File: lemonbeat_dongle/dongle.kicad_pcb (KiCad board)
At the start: 4 copper layers, 50 x 20 mm, 81 parts, among them J201 USB_A, J202 Prog, J203 u.FL, J301 SMA, SW201 SW_Push, U201 nRF52840, U301 Si4467, Y201 32MHz, Y202 32.768kHz, Y301 26MHz

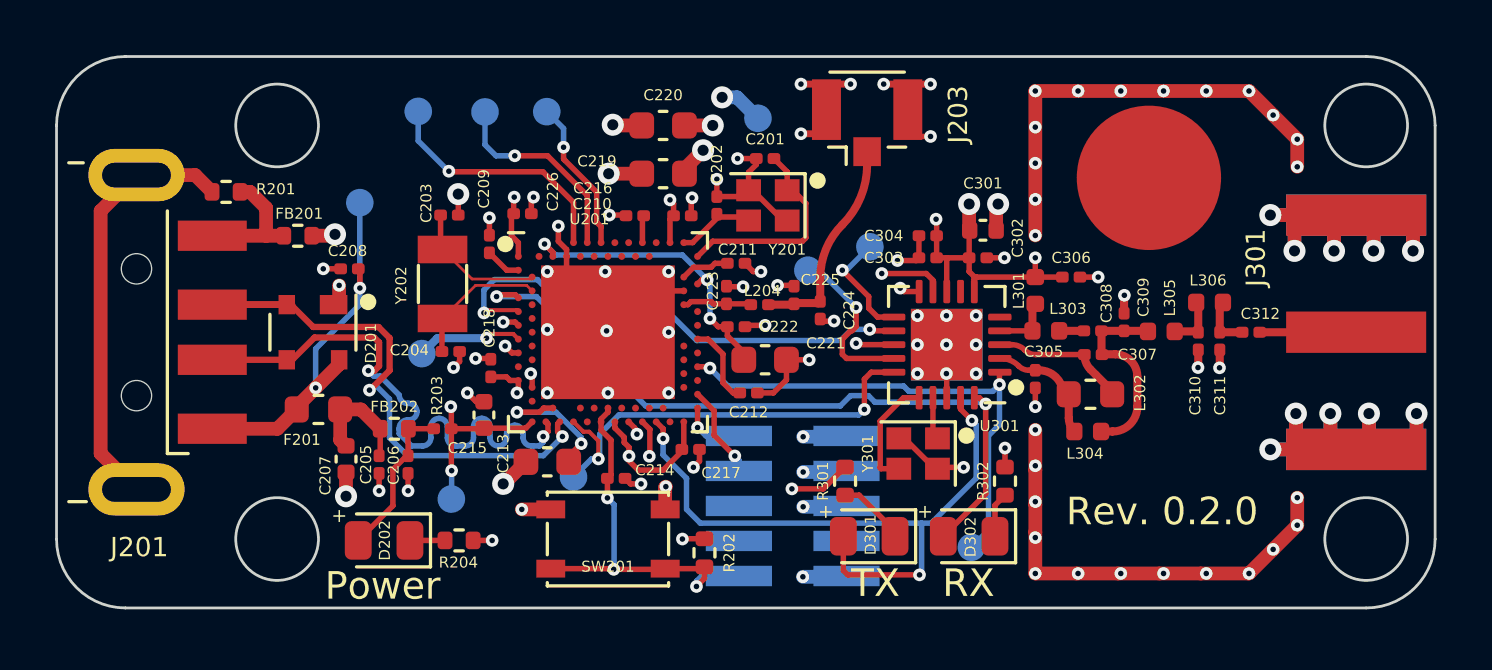
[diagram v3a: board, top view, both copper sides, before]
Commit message: dongle: PCB: move components further away from holes
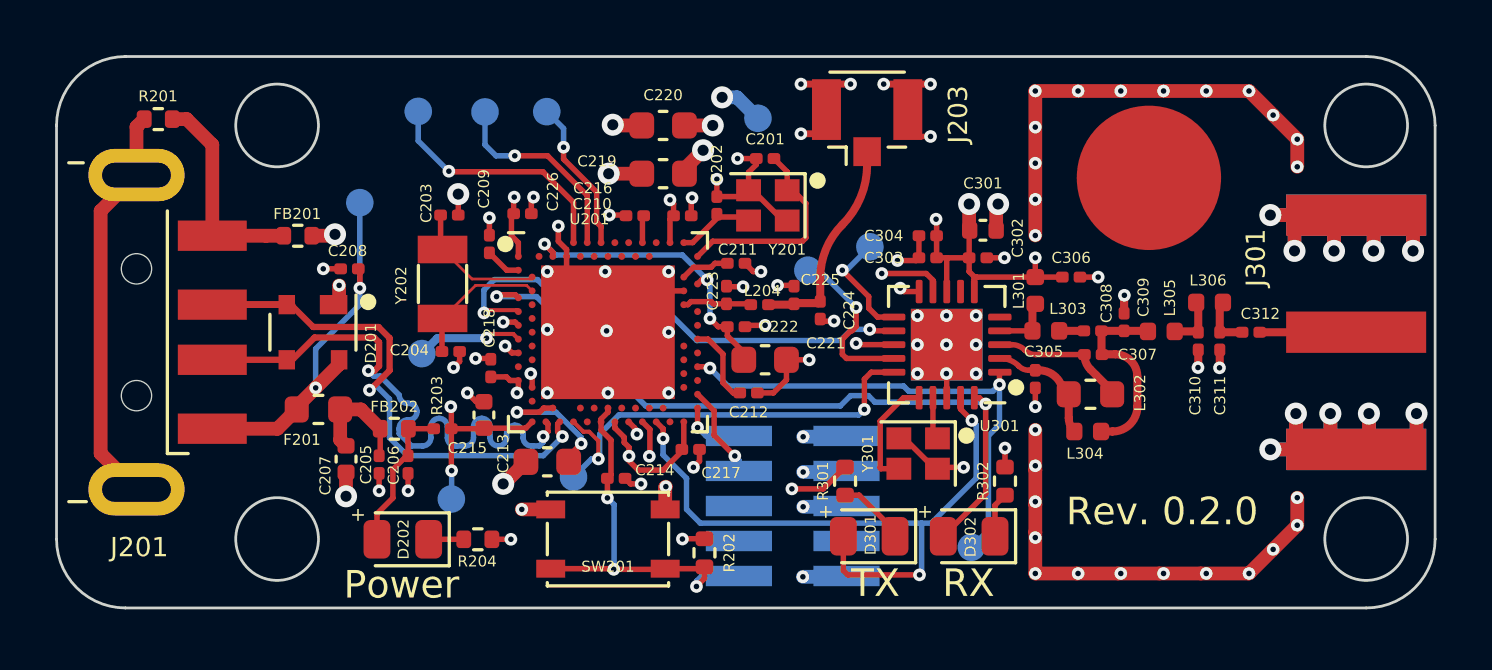
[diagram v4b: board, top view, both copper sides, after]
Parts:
- moved R201 3.61 mm to (114.2, 96.3)
- moved D202 0.68 mm to (123.1, 111.5)
- moved R204 0.68 mm to (125.8, 111.5)
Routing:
- net Net-(FB201-Pad1): track 4.58 -> 7.53 mm
- net Net-(J201-Pad5): track 15.5 -> 14.6 mm
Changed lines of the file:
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@@
   )
   (footprint "LED_SMD:LED_0805_2012Metric" (layer "F.Cu")
-    (at 122.38 111.55 180)
+    (at 123.06 111.51 180)
     (descr "LED SMD 0805 (2012 Metric), square (rectangular) end terminal, IPC_7351 nominal, (Body size source: https://docs.google.com/spreadsheets/d/1BsfQQcO9C6DZCsRaXUlFlo91Tg2WpOkGARC1WS5S8t0/edit?usp=sharing), generated with kicad-footprint-generator")
     (tags "LED")
@@
   )
   (footprint "Resistor_SMD:R_0402_1005Metric" (layer "F.Cu")
-    (at 125.1 111.55)
+    (at 125.78 111.51)
     (descr "Resistor SMD 0402 (1005 Metric), square (rectangular) end terminal, IPC_7351 nominal, (Body size source: IPC-SM-782 page 72, https://www.pcb-3d.com/wordpress/wp-content/uploads/ipc-sm-782a_amendment_1_and_2.pdf), generated with kicad-footprint-generator")
     (tags "resistor")
@@
   )
   (footprint "Resistor_SMD:R_0402_1005Metric" (layer "F.Cu")
-    (at 116.65 98.91)
+    (at 114.19 96.27)
     (descr "Resistor SMD 0402 (1005 Metric), square (rectangular) end terminal, IPC_7351 nominal, (Body size source: IPC-SM-782 page 72, https://www.pcb-3d.com/wordpress/wp-content/uploads/ipc-sm-782a_amendment_1_and_2.pdf), generated with kicad-footprint-generator")
     (tags "resistor")
@@
     (property "Sheetname" "MCU")
     (attr smd)
-    (fp_text reference "R201" (at 1.8 -0.1) (layer "F.SilkS")
+    (fp_text reference "R201" (at -0.01 -0.83) (layer "F.SilkS")
       (effects (font (size 0.4 0.4) (thickness 0.1)))
     )
@@
     (property "Sheetname" "MCU")
     (attr smd)
-    (fp_text reference "FB201" (at 0.05 -0.8) (layer "F.SilkS")
+    (fp_text reference "FB201" (at -0.02 -0.79) (layer "F.SilkS")
       (effects (font (size 0.4 0.4) (thickness 0.1)))
     )
@@
   (gr_arc (start 160.5 111.5) (mid 159.767767 113.267767) (end 158 114) (layer "Edge.Cuts") (width 0.1))
   (gr_line (start 113 94) (end 158 94) (layer "Edge.Cuts") (width 0.1))
-  (gr_text "Power" (at 122.33 113.2) (layer "F.SilkS")
+  (gr_text "Power" (at 123.01 113.16) (layer "F.SilkS")
     (effects (font (size 1 1) (thickness 0.15)))
   )
-  (gr_text "+" (at 120.755 110.65) (layer "F.SilkS")
+  (gr_text "+" (at 121.435 110.61) (layer "F.SilkS")
     (effects (font (size 0.5 0.5) (thickness 0.1)))
   )
@@
   (segment (start 142.7875 106.375) (end 142.7875 105.4875) (width 0.2) (layer "F.Cu") (net 1))
   (segment (start 142.7875 105.3125) (end 142.7875 104.45) (width 0.2) (layer "F.Cu") (net 1))
-  (segment (start 126.3 111.55) (end 125.61 111.55) (width 0.2) (layer "F.Cu") (net 1))
+  (segment (start 126.98 111.51) (end 126.29 111.51) (width 0.2) (layer "F.Cu") (net 1))
   (segment (start 120.7 101.7) (end 120.75 101.75) (width 0.2) (layer "F.Cu") (net 1))
   (segment (start 127.72 99.18) (end 127.8 99.1) (width 0.2) (layer "F.Cu") (net 1))
@@
   (via (at 154.625 111.875) (size 0.46) (drill 0.2) (layers "F.Cu" "B.Cu") (free) (net 1))
   (via (at 125.7 104.95) (size 0.46) (drill 0.2) (layers "F.Cu" "B.Cu") (free) (net 1))
-  (via (at 126.3 111.55) (size 0.46) (drill 0.2) (layers "F.Cu" "B.Cu") (free) (net 1))
+  (via (at 126.98 111.51) (size 0.46) (drill 0.2) (layers "F.Cu" "B.Cu") (free) (net 1))
   (via (at 126.2 99.85) (size 0.46) (drill 0.2) (layers "F.Cu" "B.Cu") (free) (net 1))
   (via (at 136.05 101.8) (size 0.46) (drill 0.2) (layers "F.Cu" "B.Cu") (free) (net 1))
@@
   (segment (start 120.7875 106.8) (end 120.7875 107.9075) (width 0.5) (layer "F.Cu") (net 6))
   (segment (start 123.25 107.51) (end 123.26 107.5) (width 0.2) (layer "F.Cu") (net 7))
-  (segment (start 122.7 108.977552) (end 122.7 110.2925) (width 0.2) (layer "F.Cu") (net 7))
-  (segment (start 122.7 110.2925) (end 121.4425 111.55) (width 0.2) (layer "F.Cu") (net 7))
+  (segment (start 122.7 108.977552) (end 123.197552 108.48) (width 0.2) (layer "F.Cu") (net 7))
+  (segment (start 122.1225 110.5875) (end 122.7 110.01) (width 0.2) (layer "F.Cu") (net 7))
   (segment (start 123.26 107.5) (end 124.18 107.5) (width 0.2) (layer "F.Cu") (net 7))
   (segment (start 123.25 108.48) (end 123.25 107.51) (width 0.2) (layer "F.Cu") (net 7))
-  (segment (start 123.197552 108.48) (end 122.7 108.977552) (width 0.2) (layer "F.Cu") (net 7))
+  (segment (start 122.1225 111.51) (end 122.1225 110.5875) (width 0.2) (layer "F.Cu") (net 7))
+  (segment (start 122.7 110.01) (end 122.7 108.977552) (width 0.2) (layer "F.Cu") (net 7))
   (segment (start 119.2125 106.8) (end 119.2125 106.704908) (width 0.5) (layer "F.Cu") (net 8))
   (segment (start 120.75 105) (end 120.75 105.167408) (width 0.5) (layer "F.Cu") (net 8))
@@
   (segment (start 122.094359 105.943545) (end 122.006455 105.943545) (width 0.2) (layer "B.Cu") (net 28))
   (segment (start 116.35 100.5) (end 118.1 100.5) (width 0.5) (layer "F.Cu") (net 29))
-  (segment (start 117.52 98.91) (end 117.16 98.91) (width 0.5) (layer "F.Cu") (net 29))
-  (segment (start 118.1 99.49) (end 117.52 98.91) (width 0.5) (layer "F.Cu") (net 29))
-  (segment (start 118.1 100.5) (end 118.1 99.49) (width 0.5) (layer "F.Cu") (net 29))
+  (segment (start 115.22 96.27) (end 116.15 97.2) (width 0.5) (layer "F.Cu") (net 29))
+  (segment (start 114.7 96.27) (end 115.22 96.27) (width 0.5) (layer "F.Cu") (net 29))
+  (segment (start 116.15 97.2) (end 116.15 100.5) (width 0.5) (layer "F.Cu") (net 29))
   (segment (start 118.1 100.5) (end 118.74 100.5) (width 0.5) (layer "F.Cu") (net 29))
   (segment (start 112.1 99.6) (end 113.4 98.3) (width 0.5) (layer "F.Cu") (net 30))
   (segment (start 113.4 109.7) (end 112.1 108.4) (width 0.5) (layer "F.Cu") (net 30))
-  (segment (start 115.53 98.3) (end 116.14 98.91) (width 0.5) (layer "F.Cu") (net 30))
+  (segment (start 113.4 96.55) (end 113.68 96.27) (width 0.5) (layer "F.Cu") (net 30))
   (segment (start 112.1 108.4) (end 112.1 99.6) (width 0.5) (layer "F.Cu") (net 30))
-  (segment (start 113.4 98.3) (end 115.53 98.3) (width 0.5) (layer "F.Cu") (net 30))
+  (segment (start 113.4 98.3) (end 113.4 96.55) (width 0.5) (layer "F.Cu") (net 30))
   (segment (start 133.75 107.4565) (end 133.75 106.75) (width 0.2) (layer "F.Cu") (net 31))
   (via (at 133.75 107.4565) (size 0.46) (drill 0.2) (layers "F.Cu" "B.Cu") (net 31))
@@
   (segment (start 140.777 104.231744) (end 139.824744 105.184) (width 0.2) (layer "In2.Cu") (net 39))
   (segment (start 138.852256 104.861) (end 138.639 104.861) (width 0.2) (layer "In2.Cu") (net 39))
-  (segment (start 123.3175 111.55) (end 124.59 111.55) (width 0.2) (layer "F.Cu") (net 40))
+  (segment (start 123.9975 111.51) (end 125.27 111.51) (width 0.2) (layer "F.Cu") (net 40))
   (segment (start 140.9125 111.4) (end 140.9125 111.2125) (width 0.2) (layer "F.Cu") (net 41))
   (segment (start 139.61 109.91) (end 139.1 109.91) (width 0.2) (layer "F.Cu") (net 41))

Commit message: dongle: schematic & PCB: nRF52840 oscillator changes
- change footprint of capacitors for both crystals to 0402 so they can
  be exchanged more easily
- rotate Y201 for better symmetry
- no ground plane keepout area below crystals
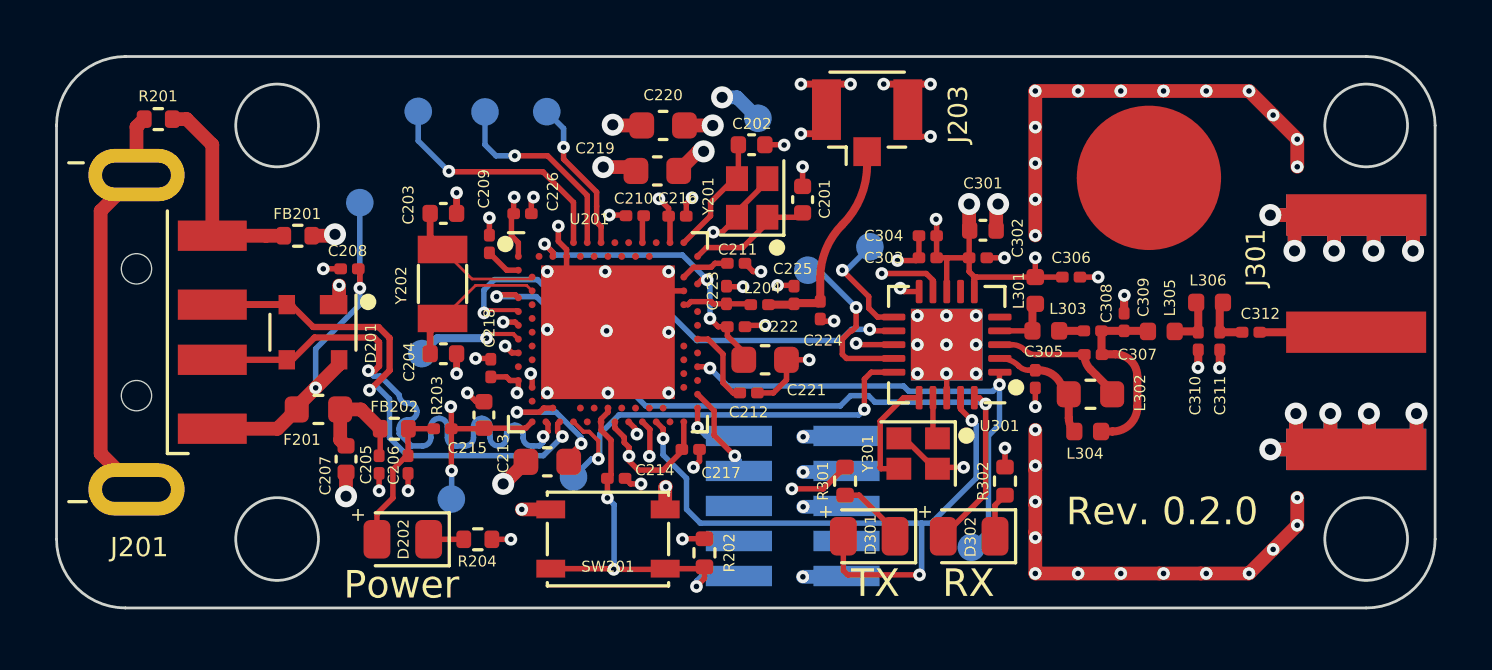
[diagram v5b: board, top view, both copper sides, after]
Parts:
- C201, C202, C203, C204: footprint Capacitor_SMD:C_0201_0603Metric -> Capacitor_SMD:C_0402_1005Metric
- moved C202 2.54 mm to (135.7, 97.2), turned to 180 degrees
- moved C201 2.02 mm to (137.6, 99.2), turned to -90 degrees
- moved Y201 0.63 mm to (135.7, 99.1), turned to 90 degrees
- moved C204 0.28 mm to (124.5, 104.8)
- moved C219 0.23 mm to (132.3, 98.2)
- moved C203 0.23 mm to (124.5, 99.7)
- moved C216 0.18 mm to (133.0, 99.8)
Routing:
- net Net-(C201-Pad2): track 7.68 -> 4.58 mm
- net Net-(C202-Pad2): track 2.79 -> 4.43 mm
- net GND: track 121.8 -> 120.7 mm, vias 105 -> 106

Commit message: dongle: add test point for SWDCLK & space test points further apart
This should allow creating a test jig even with test pads of 2mm
diameter.
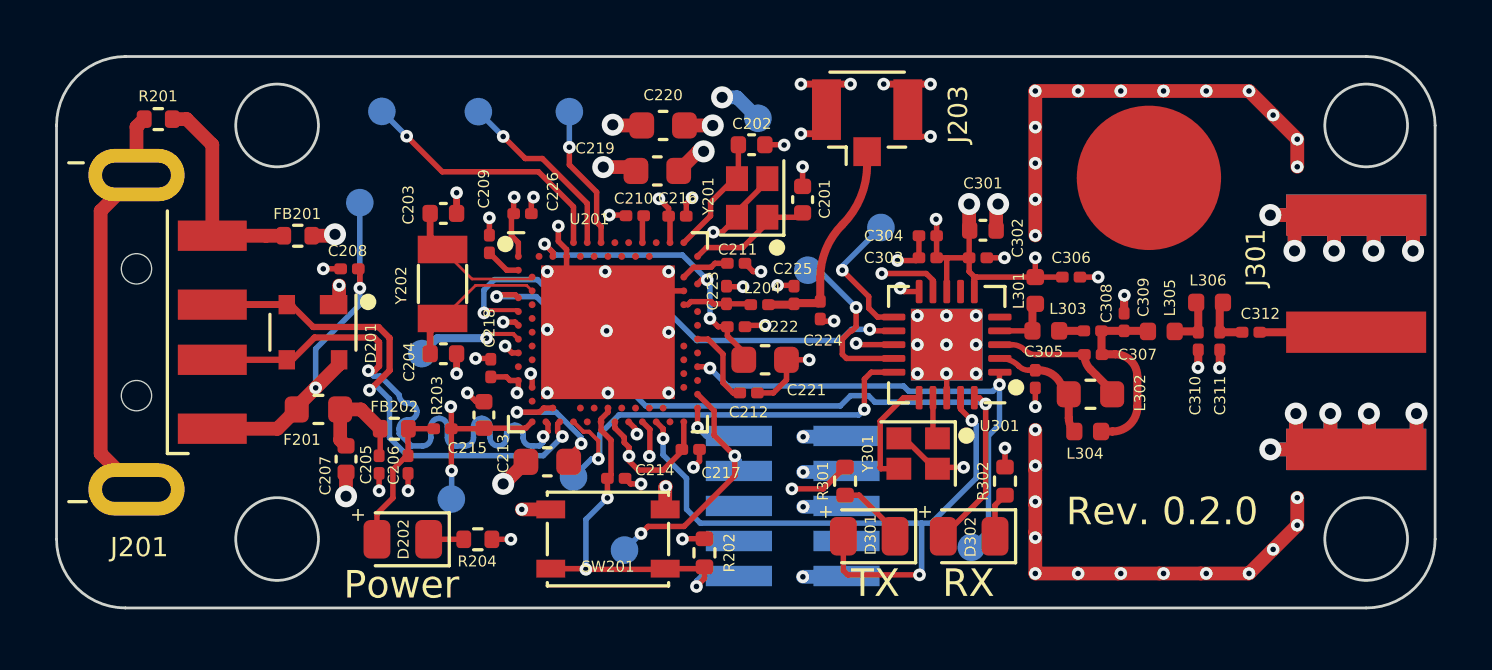
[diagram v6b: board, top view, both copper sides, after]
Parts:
- added TP207: TestPoint, TestPoint:TestPoint_Pad_D1.0mm, B.Cu at (131.1, 111.9)
- moved TP206 1.32 mm to (122.3, 96.0)
- moved TP204 0.82 mm to (129.1, 96.0)
- moved TP106 0.81 mm to (140.4, 100.2)
- moved TP205 0.24 mm to (125.8, 96.0)
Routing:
- net /MCU/SWDCLK: track 3.40 -> 9.24 mm, vias 1 -> 2
- net /MCU/P1.09: track 19.0 -> 19.7 mm
- net Net-(TP205-Pad1): track 7.37 -> 6.75 mm
- net Net-(TP206-Pad1): track 9.08 -> 9.68 mm

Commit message: dongle: update schematics & PCBs to KiCAD 7 & fix ERC/DRC errors & warnings
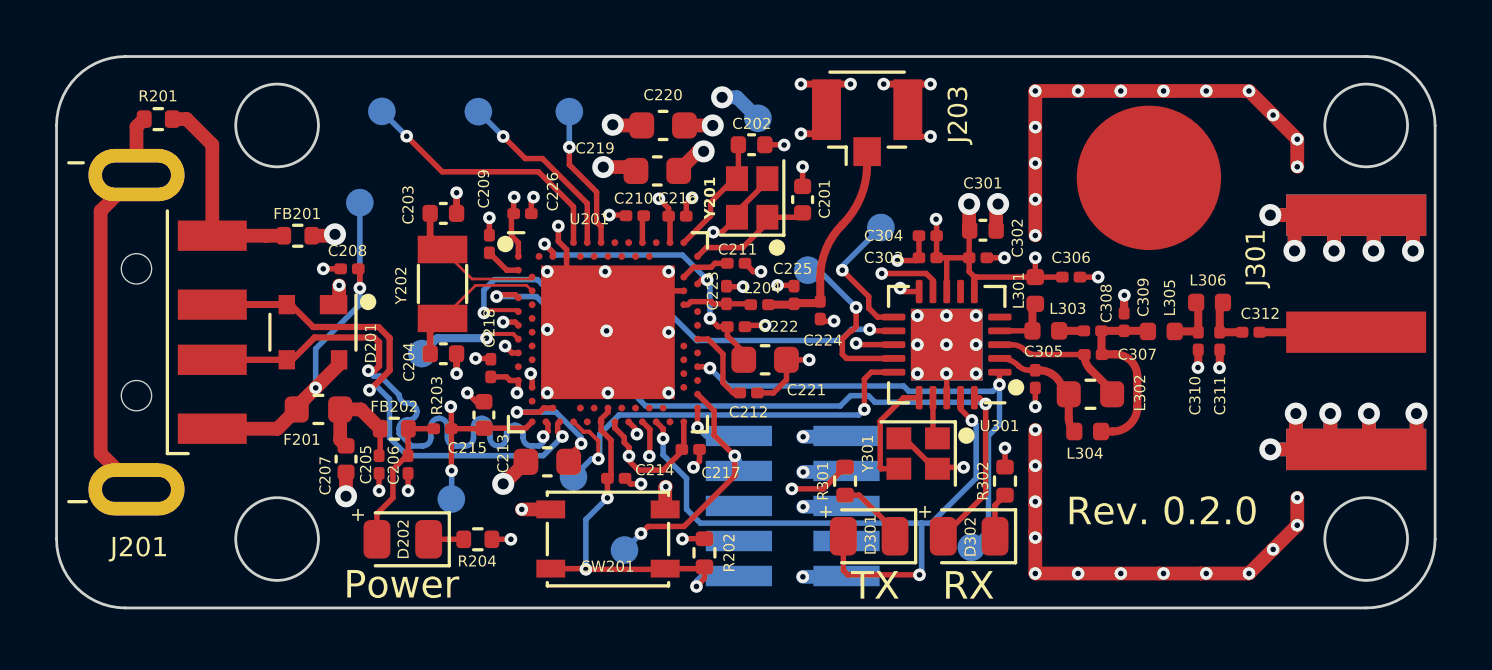
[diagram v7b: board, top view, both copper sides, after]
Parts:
- G1: footprint custom_library:smart_tulip_soldermask -> Logos:smart_tulip_soldermask
